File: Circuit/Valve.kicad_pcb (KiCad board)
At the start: 2 copper layers, 95 x 72.1 mm, 22 parts, among them CN1 GROVE, CN2 ST-LINK, CN3 TTL-232R-3V3, J1 Conn_01x04_Male, SW1 RESET, U1 STM32L010F4P6

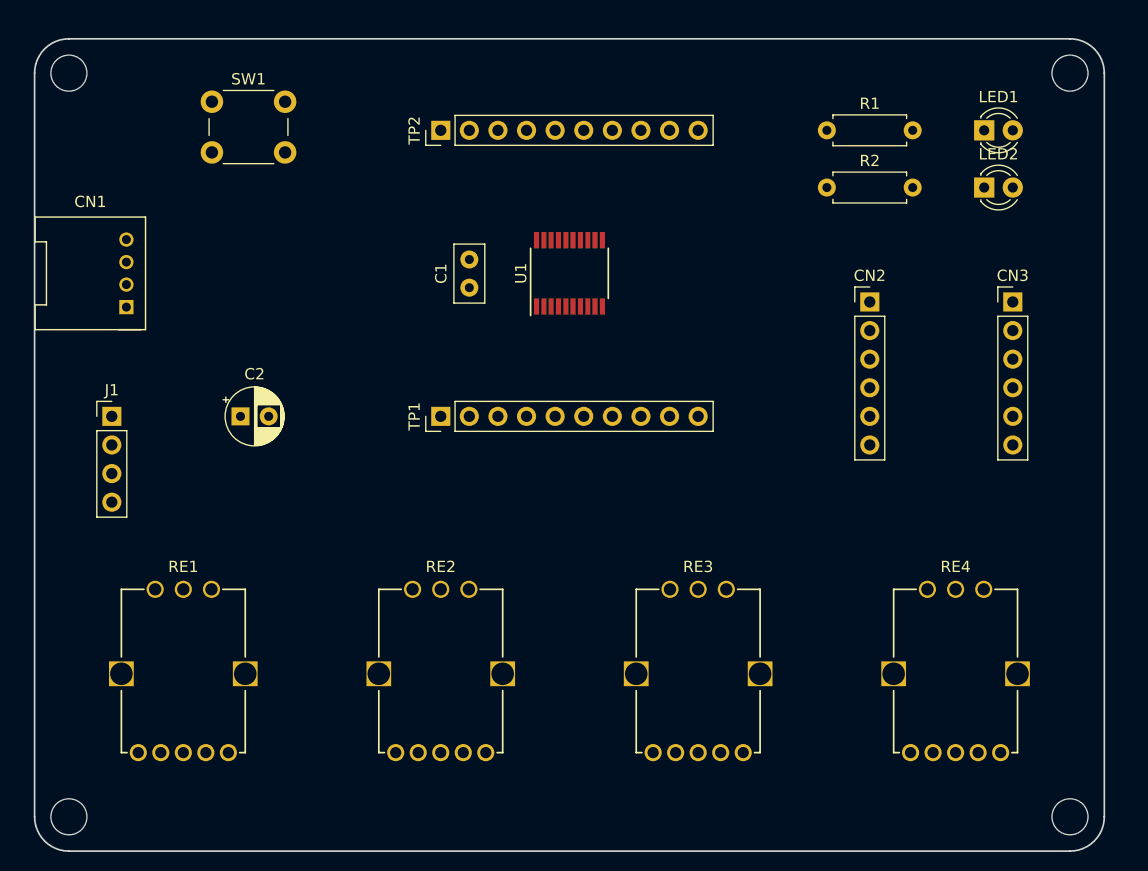
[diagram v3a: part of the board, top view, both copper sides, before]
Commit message: フットプリントに説明シルクを追加
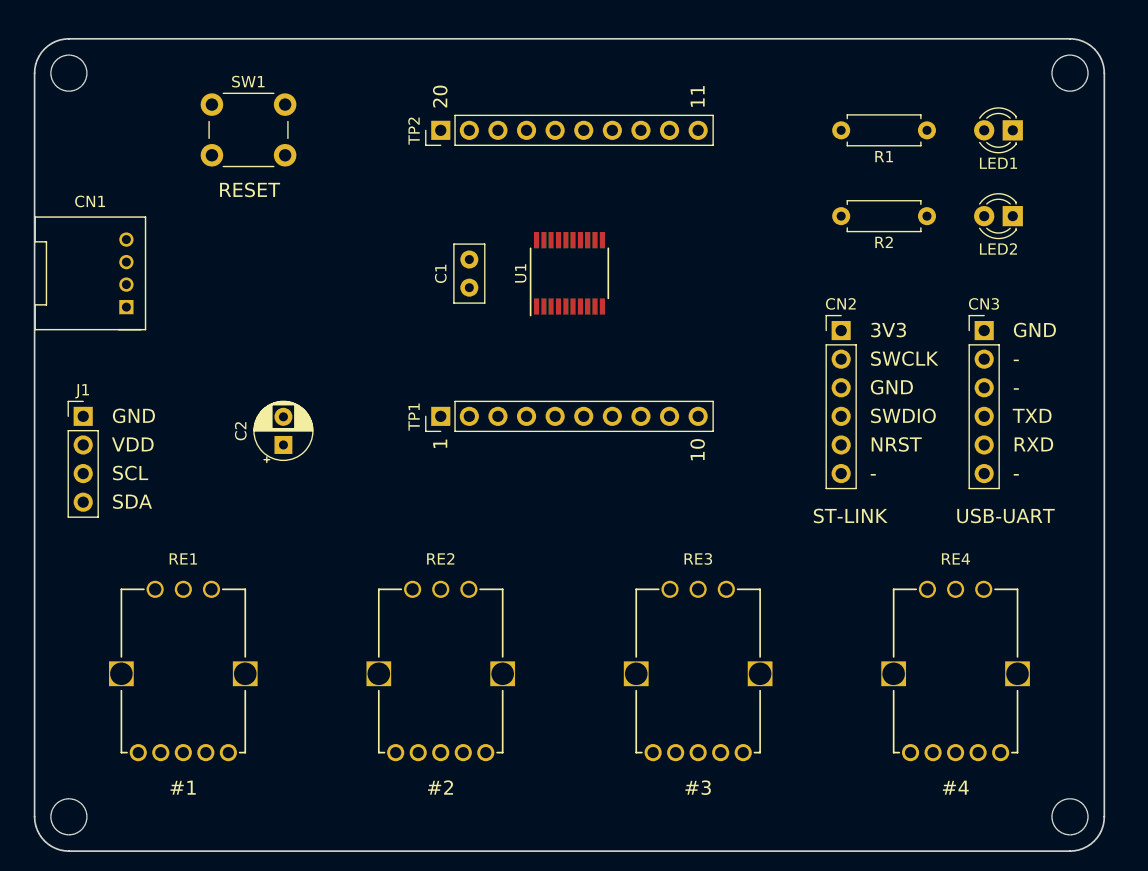
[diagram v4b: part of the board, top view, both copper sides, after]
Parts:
- moved R2 9.25 mm to (152.4, 63.5), turned to 180 degrees
- moved R1 8.89 mm to (152.4, 55.9), turned to 180 degrees
- moved C2 4.58 mm to (95.2, 83.8), turned to 90 degrees
- moved LED2 3.59 mm to (160.0, 63.5), turned to 180 degrees
- moved CN3 3.59 mm to (157.5, 73.7)
- moved CN2 3.59 mm to (144.8, 73.7)
- moved LED1 2.54 mm to (160.0, 55.9), turned to 180 degrees
- moved J1 2.54 mm to (77.5, 81.3)
- moved SW1 0.25 mm to (88.9, 53.6)
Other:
- board text added: "#1"
- board text added: "#2"
- board text added: "#3"
- board text added: "#4"
- board text added: "-"
- board text added: "1"
- board text added: "10"
- board text added: "11"
- board text added: "20"
- board text added: "3V3"
- board text added: "GND"
- board text added: "NRST"
- board text added: "RESET"
- board text added: "RXD"
- board text added: "SCL"
- board text added: "SDA"
- board text added: "ST-LINK"
- board text added: "SWCLK"
- board text added: "SWDIO"
- board text added: "TXD"
- board text added: "USB-UART"
- board text added: "VDD"

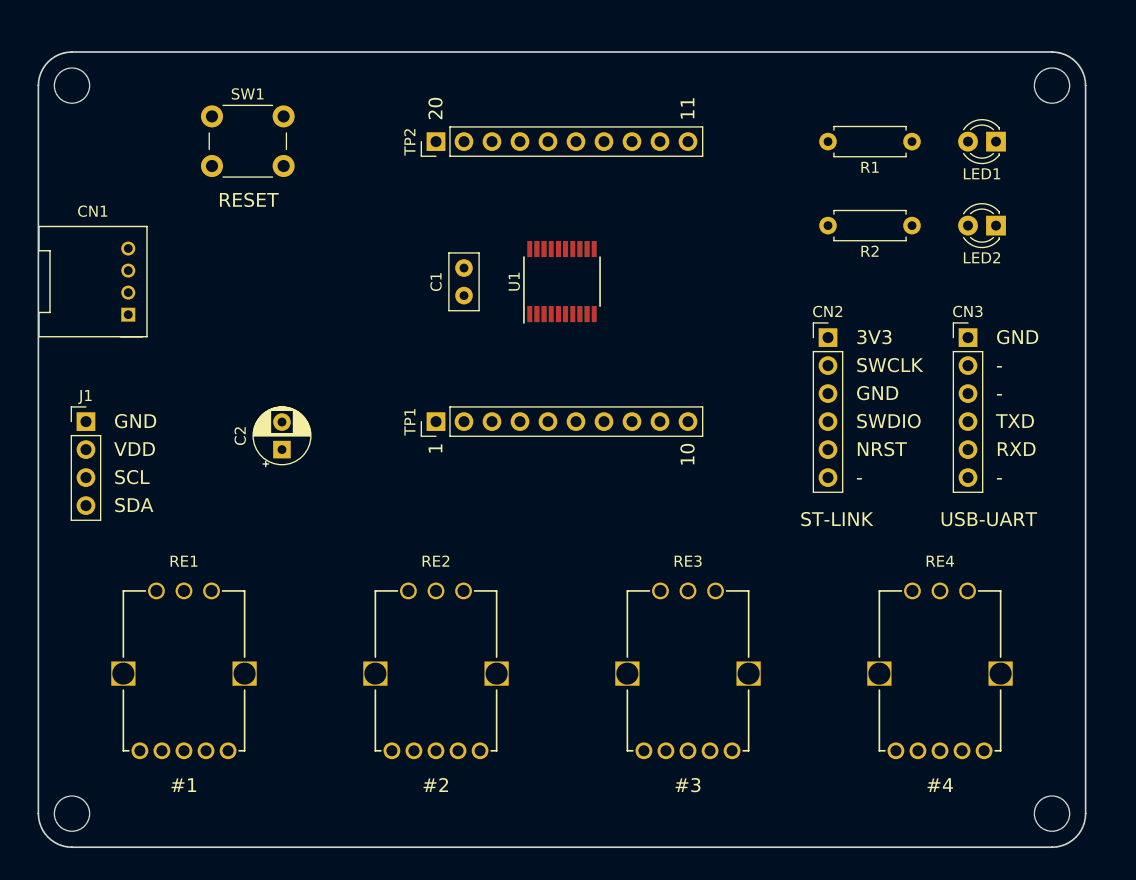
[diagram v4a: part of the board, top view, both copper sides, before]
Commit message: I2C プルアップ抵抗 (DNP) を追加
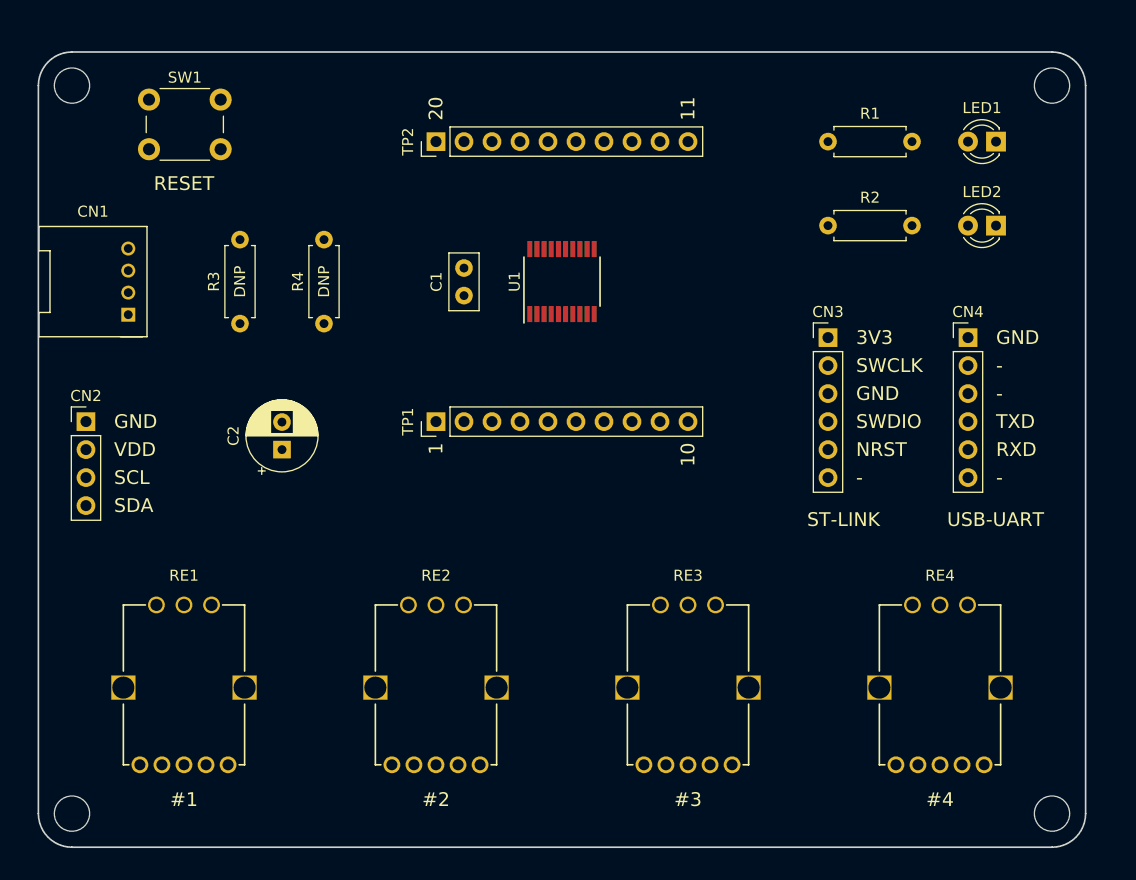
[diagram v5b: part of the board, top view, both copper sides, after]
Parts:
- removed J1: Conn_01x04_Male, Connector_PinHeader_2.54mm:PinHeader_1x04_P2.54mm_Vertical
- added CN4: TTL-232R-3V3, Connector_PinHeader_2.54mm:PinHeader_1x06_P2.54mm_Vertical, F.Cu at (157.5, 73.7)
- added R3: N/A, Resistor_THT:R_Axial_DIN0207_L6.3mm_D2.5mm_P7.62mm_Horizontal, F.Cu at (91.4, 72.4)
- added R4: N/A, Resistor_THT:R_Axial_DIN0207_L6.3mm_D2.5mm_P7.62mm_Horizontal, F.Cu at (99.1, 72.4)
- C2: value 47u -> 100u; footprint Capacitor_THT:CP_Radial_D5.0mm_P2.50mm -> Capacitor_THT:CP_Radial_D6.3mm_P2.50mm
- CN2: value ST-LINK -> Conn_01x04_Male; footprint Connector_PinHeader_2.54mm:PinHeader_1x06_P2.54mm_Vertical -> Connector_PinHeader_2.54mm:PinHeader_1x04_P2.54mm_Vertical
- CN3: value TTL-232R-3V3 -> ST-LINK
- moved CN2 67.7 mm to (77.5, 81.3)
- moved CN3 12.7 mm to (144.8, 73.7)
- moved SW1 5.91 mm to (83.2, 52.1)
- moved RE1 1.27 mm to (86.4, 105.4)
- moved RE2 1.27 mm to (109.2, 105.4)
- moved RE3 1.27 mm to (132.1, 105.4)
- moved RE4 1.27 mm to (154.9, 105.4)
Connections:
- CN2 pad 1: VDD -> GND
- CN2 pad 2: SWCLK -> VDD
- CN2 pad 3: GND -> SCL
- CN2 pad 4: SWDIO -> SDA
- CN3 pad 1: GND -> VDD
- CN3 pad 2: Net-(CN3-Pad2) -> SWCLK
- CN3 pad 3: Net-(CN3-Pad3) -> GND
- CN3 pad 4: TXD -> SWDIO
- CN3 pad 5: RXD -> NRST
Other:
- board text added: "DNP"

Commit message: 配線の全体仮組み
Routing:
- net GND: track 0.00 -> 224.0 mm
- net /PC14: track 0.00 -> 137.1 mm
- net /PC15: track 0.00 -> 129.6 mm
- net /PA5: track 0.00 -> 123.9 mm
- net VDD: track 0.00 -> 121.3 mm
- net /PA6: track 0.00 -> 117.8 mm
- net /PA7: track 0.00 -> 116.2 mm
- net /PB1: track 0.00 -> 110.8 mm
- net SDA: track 0.00 -> 90.7 mm
- net SCL: track 0.00 -> 87.0 mm
- net NRST: track 0.00 -> 80.5 mm, vias 0 -> 2
- net /PA4: track 0.00 -> 74.8 mm
- net /PA3: track 0.00 -> 63.0 mm
- net TXD: track 0.00 -> 52.8 mm
- net RXD: track 0.00 -> 50.7 mm, vias 0 -> 1
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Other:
- board text added: "@ext_sui 2022.01"
- board text added: "Valve v1.0"

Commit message: 配線を一通り接続完了
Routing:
- net /PB9: track 13.3 -> 50.9 mm, vias 0 -> 1
- net /PA5: track 123.9 -> 86.4 mm
- net /PA7: track 116.2 -> 79.2 mm
- net /PB1: track 110.8 -> 74.6 mm
- net /PA6: track 117.8 -> 82.2 mm
- net VDD: track 121.3 -> 147.4 mm, vias 0 -> 1
- net GND: track 224.0 -> 237.5 mm, vias 0 -> 4
- net RXD: track 50.7 -> 56.2 mm
- net SCL: track 87.0 -> 81.5 mm
- net /PA4: track 74.8 -> 69.8 mm
- net /PC15: track 129.6 -> 124.6 mm
- net /PC14: track 137.1 -> 133.0 mm
- net SDA: track 90.7 -> 94.6 mm, vias 0 -> 1
- net /PA3: track 63.0 -> 60.1 mm
- net SWDIO: track 48.8 -> 47.1 mm
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
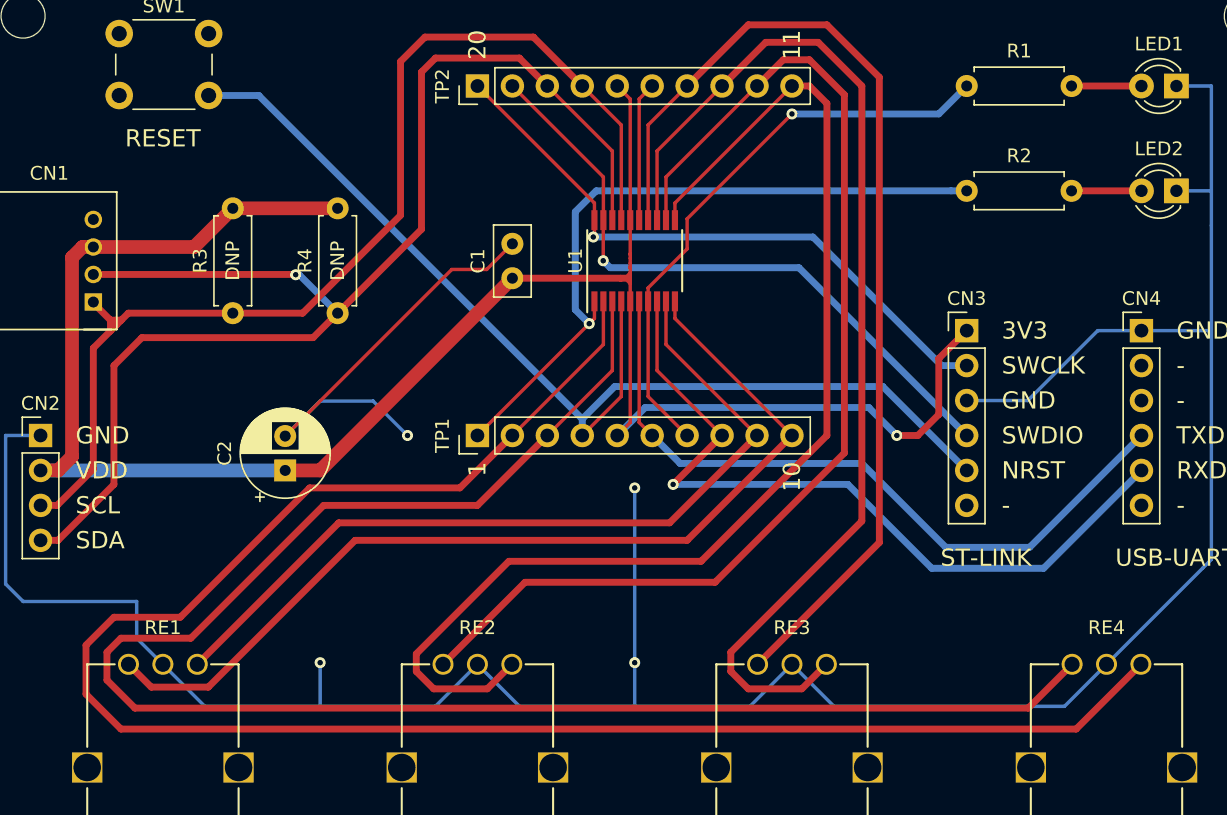
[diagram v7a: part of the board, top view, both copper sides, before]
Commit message: U1 と TP1,2 間の配線を微細化
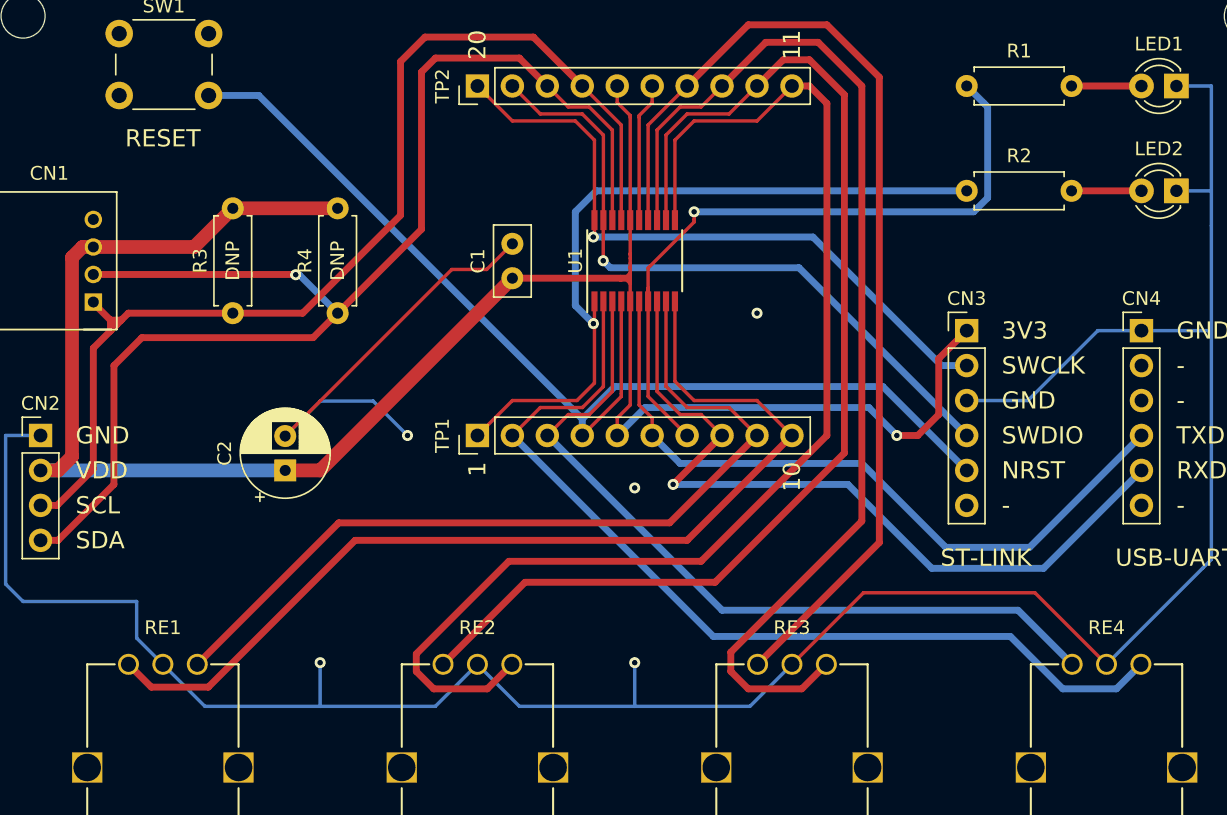
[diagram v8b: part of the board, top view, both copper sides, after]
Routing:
- net /PC15: track 124.6 -> 57.6 mm
- net /PC14: track 133.0 -> 68.3 mm
- net GND: track 237.5 -> 226.6 mm, vias 4 -> 5
- net /PA1: track 42.4 -> 50.3 mm
- net /PB9: track 50.9 -> 53.9 mm
- net /PA5: track 86.4 -> 89.0 mm
- net SWCLK: track 45.5 -> 48.2 mm
- net /PA4: track 69.8 -> 72.4 mm
- net SWDIO: track 47.1 -> 48.9 mm
- net /PA6: track 82.2 -> 84.0 mm
- net /PA3: track 60.1 -> 61.8 mm
- net SDA: track 94.6 -> 95.5 mm
- net RXD: track 56.2 -> 57.1 mm
- net /PA7: track 79.2 -> 80.1 mm
